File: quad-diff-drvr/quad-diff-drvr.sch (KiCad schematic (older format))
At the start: 46 parts, among them J1 Raspberry_Pi_2_3, J2 Conn_01x04, J3 Conn_01x04, J4 Conn_01x04, J5 Conn_01x04, J6 Conn_01x04, U1 INA3221, U2 74LS153, U3 74LS153, U4 74LS153, U5 PCA9555PW, U6 LTC1688

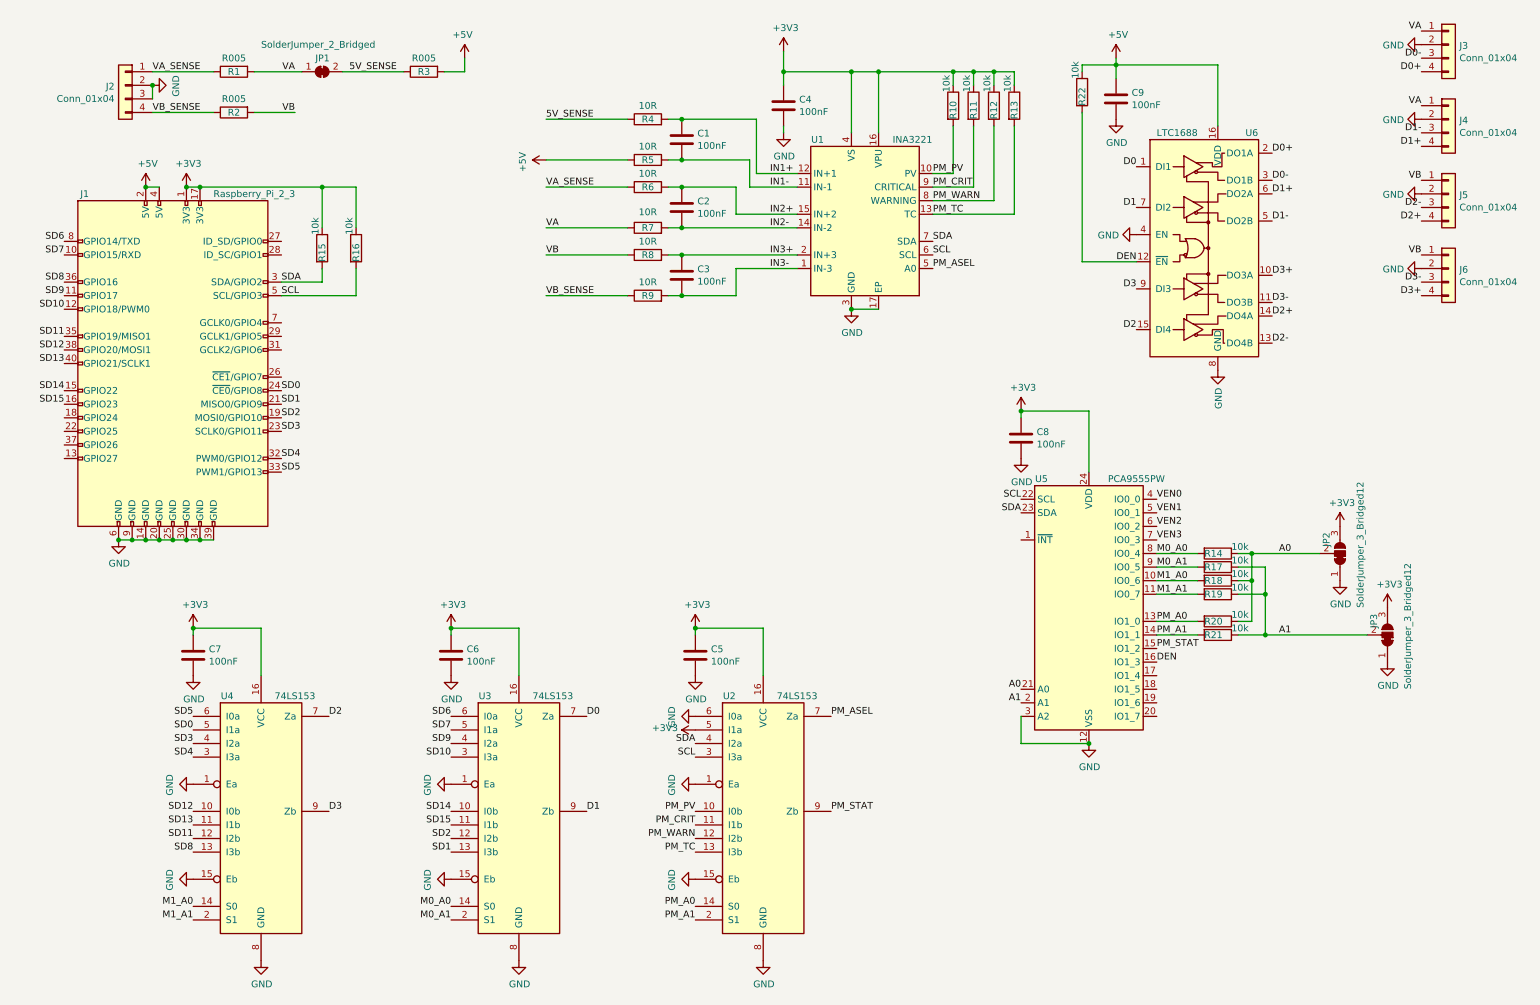
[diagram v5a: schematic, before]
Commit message: qdd: adding high-side switch
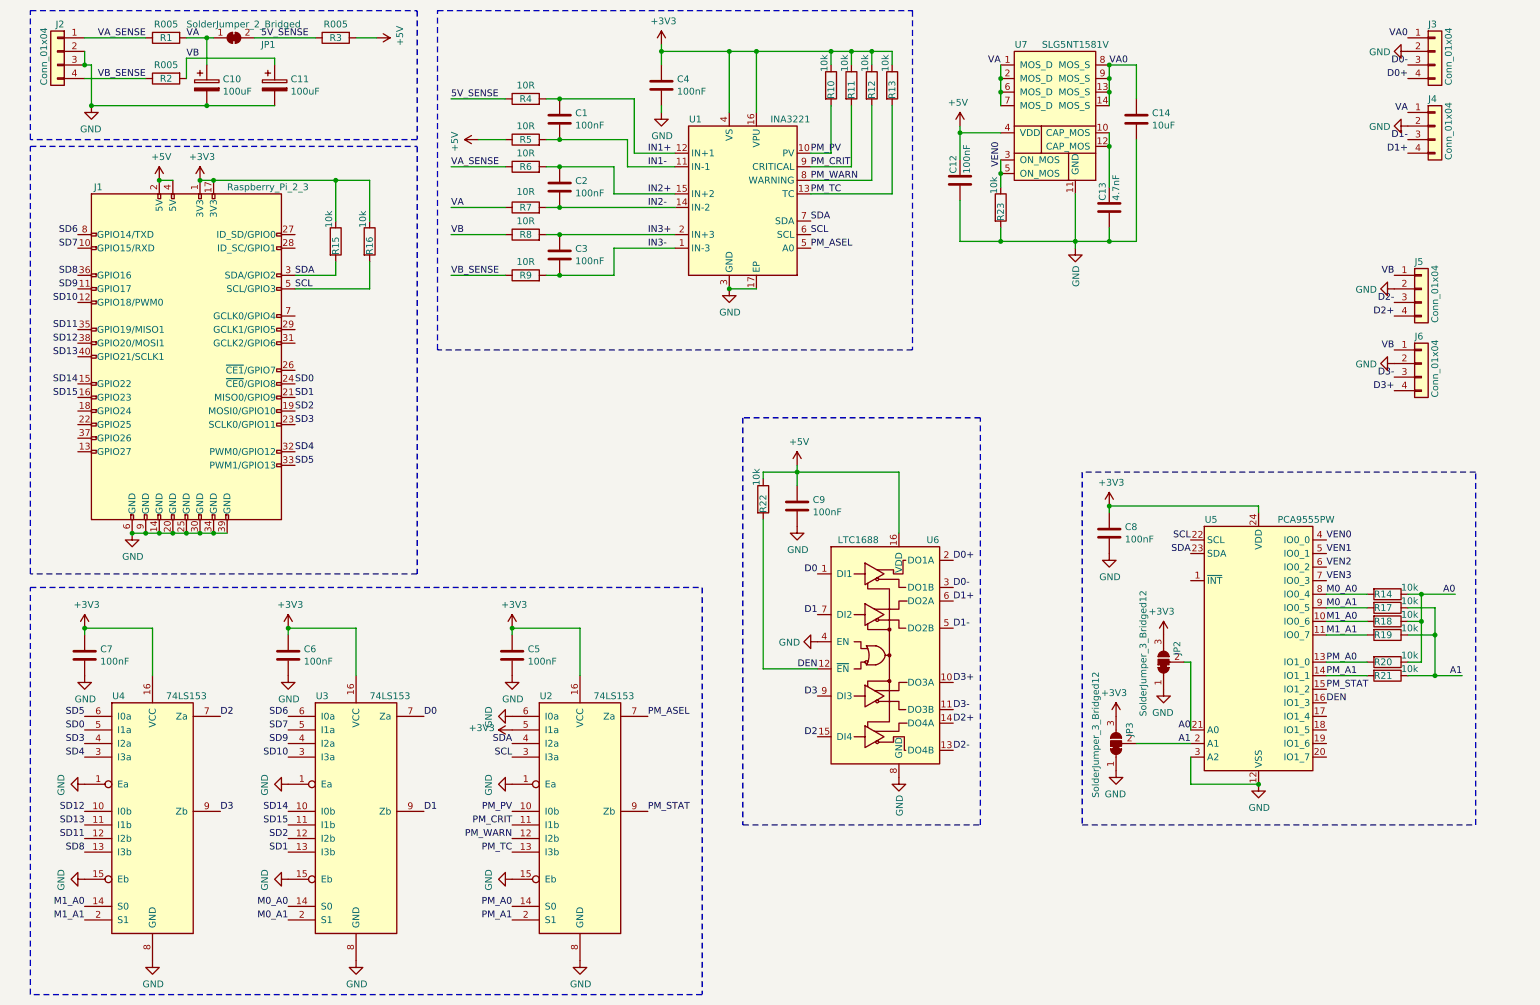
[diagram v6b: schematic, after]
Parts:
- added C10, C11: 100uF, Capacitor_SMD:CP_Elec_6.3x7.7, symbol Device:CP
- added C12: 100nF, Capacitor_SMD:C_0603_1608Metric, symbol Device:C
- added C13: 4.7nF, Capacitor_SMD:C_0603_1608Metric, symbol Device:C
- added C14: 10uF, Capacitor_SMD:C_0603_1608Metric, symbol Device:C
- added R23: 10k, Resistor_SMD:R_0603_1608Metric, symbol Device:R
- added U7: SLG5NT1581V, octo-pcb:QFN-28_1x3_Pitch0.4mm, symbol octo-pcb:SLG5NT1581V
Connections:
- net +5V: now also C12.1, U7.4 (VDD)
- net GND: now also C10.2, C11.2, C12.2, C13.2, C14.2, R23.2, U7.11 (GND)
- net VA: now also C10.1, U7.1 (MOS_D), U7.2 (MOS_D), U7.6 (MOS_D), U7.7 (MOS_D); no longer J3.1 (Pin_1)
- net VB: now also C11.1
- net VEN0: now also R23.1, U7.3 (ON_MOS), U7.5 (ON_MOS)
- new net: C13.1, U7.10 (CAP_MOS), U7.12 (CAP_MOS)
- new net VA0: C14.1, J3.1 (Pin_1), U7.13 (MOS_S), U7.14 (MOS_S), U7.8 (MOS_S), U7.9 (MOS_S)
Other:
- moved on the sheet: C1, C2, C3, C4, C5, C6, C7, C8, C9, J1, J2, J3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

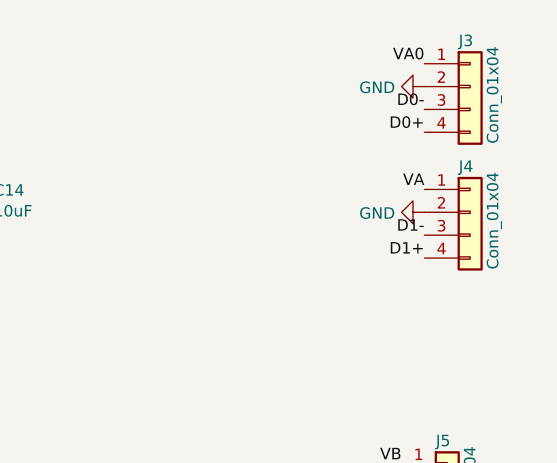
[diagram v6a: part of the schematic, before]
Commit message: qdd: unsure what got out of sync
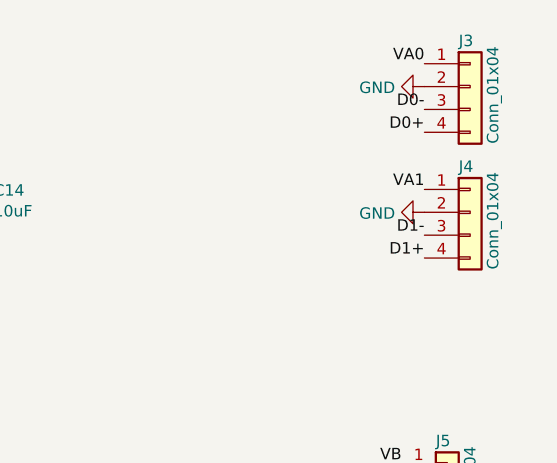
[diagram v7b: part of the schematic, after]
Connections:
- net VA: no longer J4.1 (Pin_1)
- new net VA1: J4.1 (Pin_1)
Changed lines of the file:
@@
 $EndComp
 Text Label 10650 1250 2    50   ~ 0
-VA
+VA1
 Text Label 10650 1550 2    50   ~ 0
 D1+

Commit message: qdd: stash wip
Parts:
- added C15: 100nF, Capacitor_SMD:C_0603_1608Metric, symbol Device:C
- added C16: 4.7nF, Capacitor_SMD:C_0603_1608Metric, symbol Device:C
- added C17: 10uF, Capacitor_SMD:C_0603_1608Metric, symbol Device:C
- added R24: 10k, Resistor_SMD:R_0603_1608Metric, symbol Device:R
- added U8: SLG5NT1581V, octo-pcb:QFN-28_1x3_Pitch0.4mm, symbol octo-pcb:SLG5NT1581V
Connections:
- net +5V: now also C15.1, U8.4 (VDD)
- net GND: now also C15.2, C16.2, C17.2, R24.2, U8.11 (GND)
- net VA: now also U8.1 (MOS_D), U8.2 (MOS_D), U8.6 (MOS_D), U8.7 (MOS_D)
- net VA1: now also C17.1, U8.13 (MOS_S), U8.14 (MOS_S), U8.8 (MOS_S), U8.9 (MOS_S)
- net VEN0: no longer U7.3 (ON_MOS)
- net VEN1: now also R24.1, U8.3 (ON_MOS)
- net at C13.1, U7.10 (CAP_MOS): no longer U7.12 (CAP_MOS)
- new net: C16.1, U8.12 (CAP_MOS)
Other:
- moved on the sheet: C1, C12, C13, C14, C2, C3, C4, C5, C6, C7, C9, J3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
